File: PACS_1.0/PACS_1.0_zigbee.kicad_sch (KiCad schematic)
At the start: 9 parts

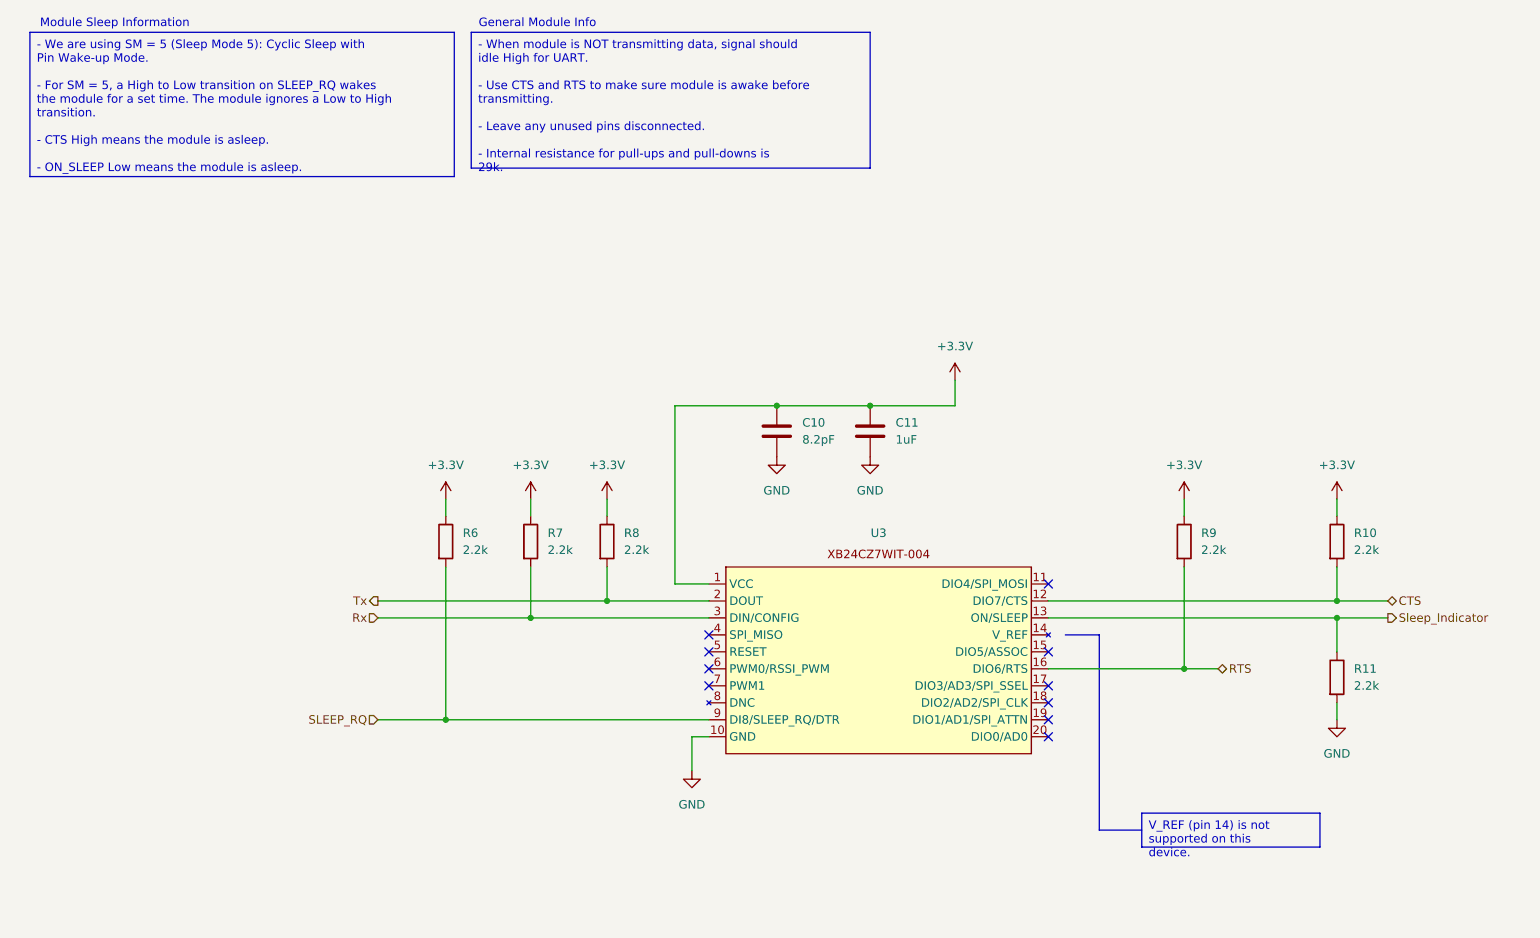
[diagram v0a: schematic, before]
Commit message: Finished 1.0 (NO INA INCLUDED)
Finished PACS 1.0 sheets, Power sheet needs considerations, no INA yet.
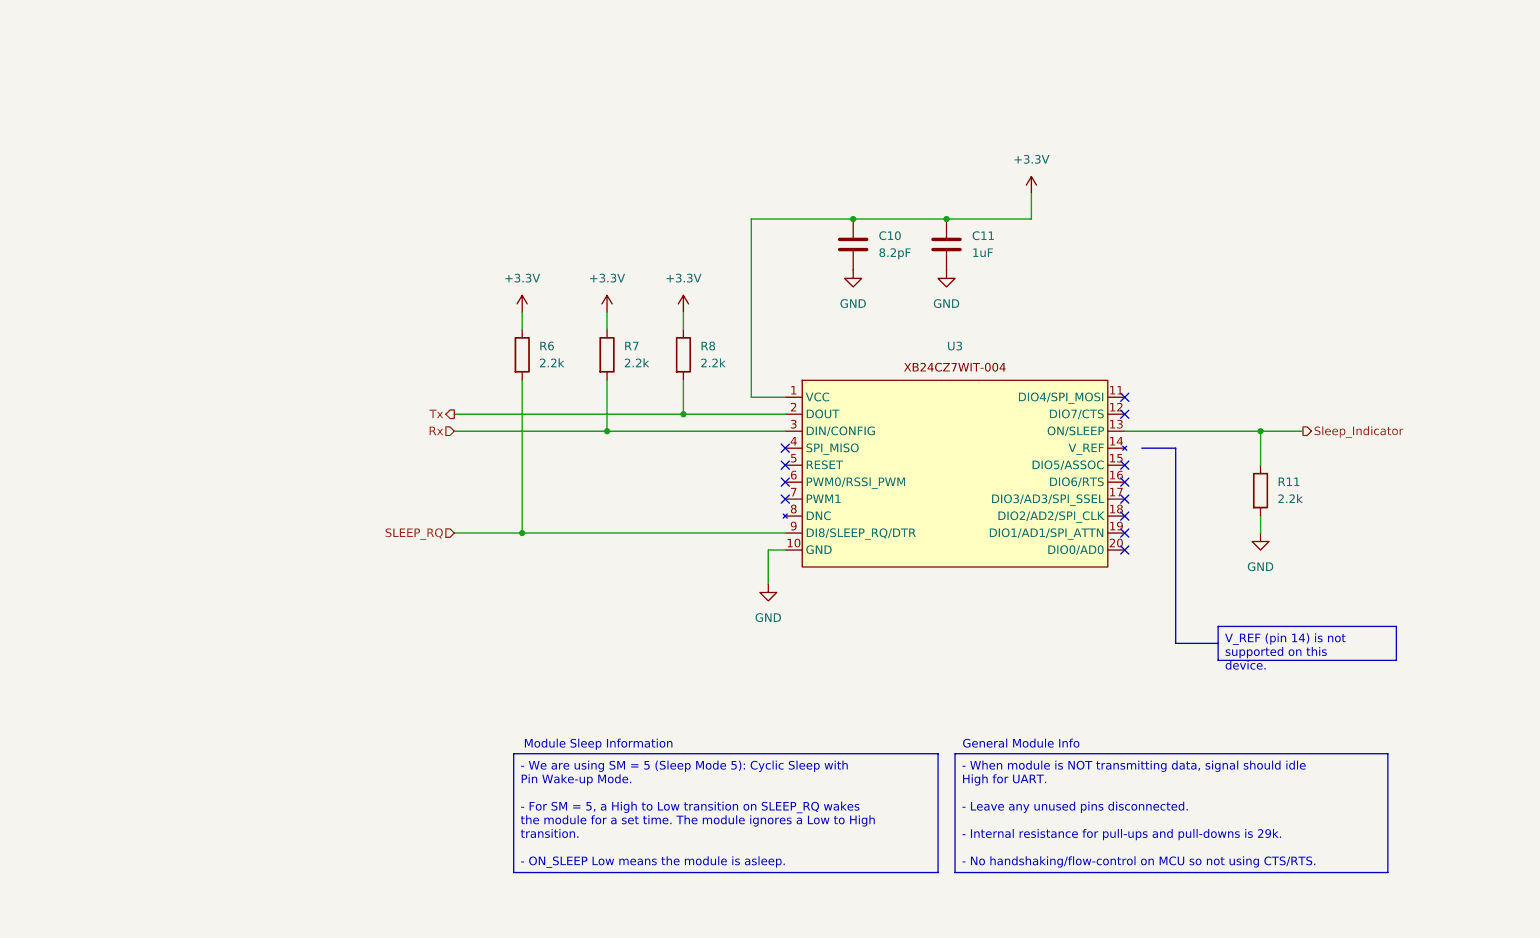
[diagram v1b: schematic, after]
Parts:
- removed R10, R9: 2.2k, symbol Device:R
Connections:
- net CTS: no longer names the net of U3.12 (DIO7/CTS)
- net RTS: no longer names the net of U3.16 (DIO6/RTS)
- no-connect marks 10 -> 12
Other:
- company: (none) -> PACS
- title: (none) -> Zigbee Module
- moved on the sheet: C10, C11, R11, R6, R7, R8, U3

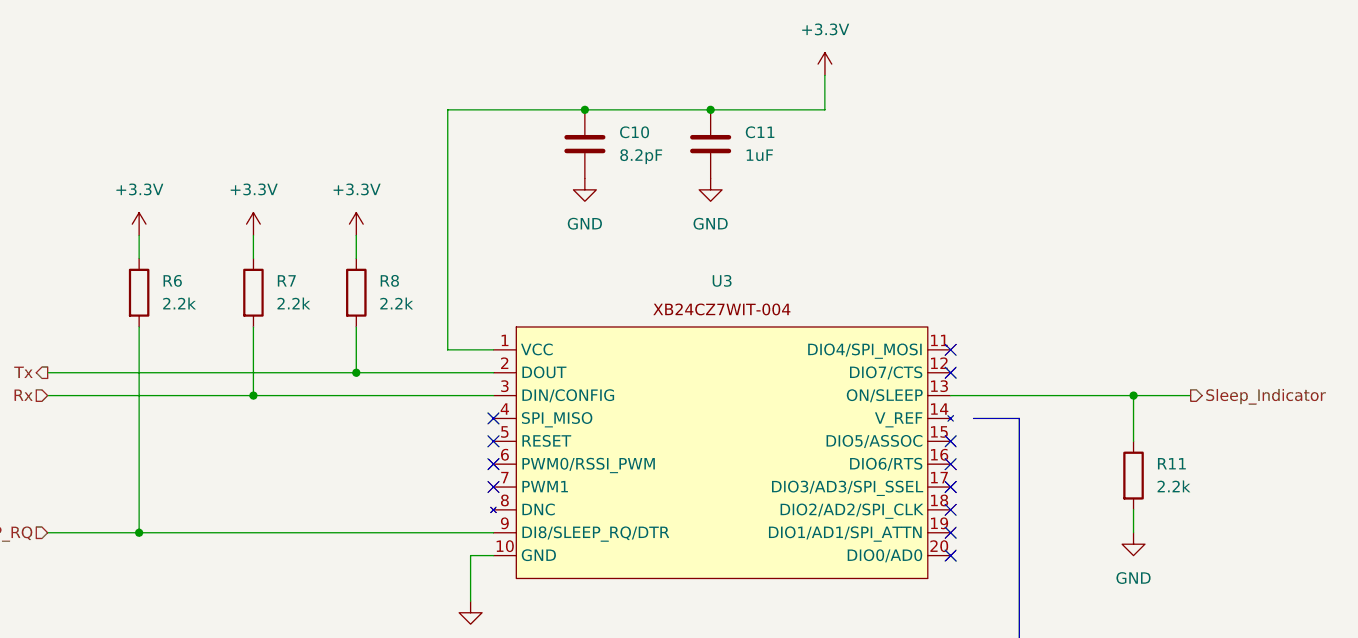
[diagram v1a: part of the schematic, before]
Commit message: Changed reference for Components
C8 to C2 (AS EXAMPLE)
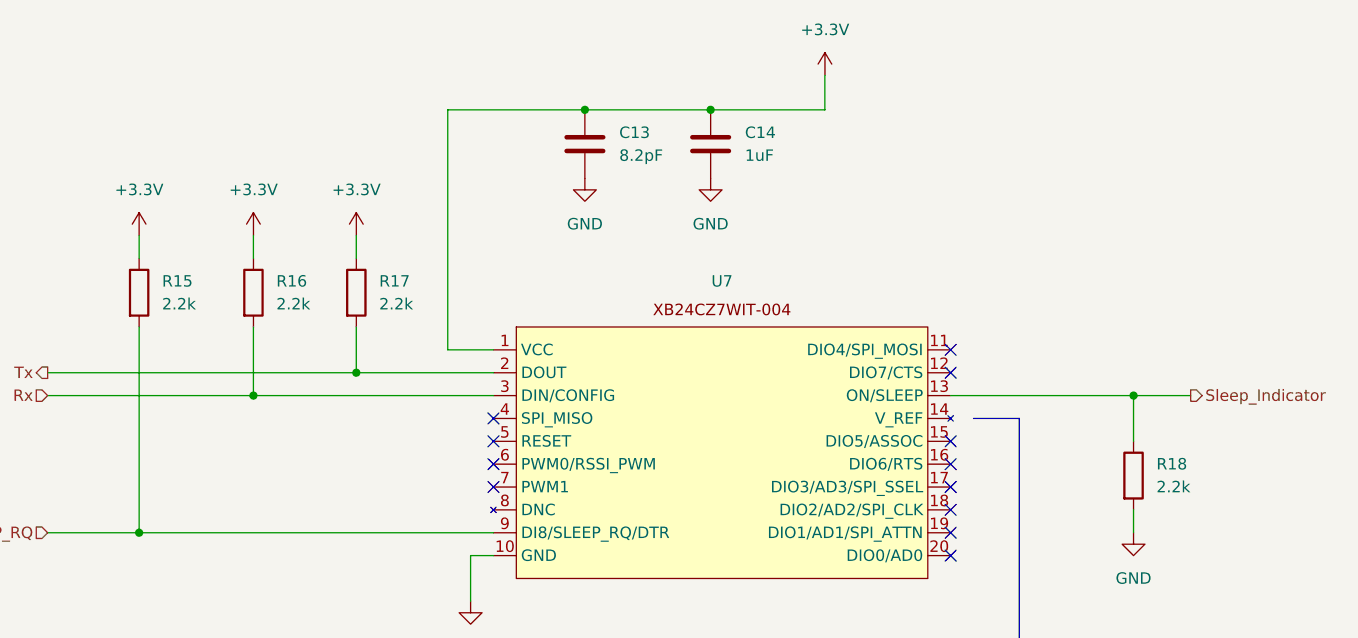
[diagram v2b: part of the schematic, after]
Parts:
- renumbered C10 to C13, C11 to C14, R6 to R15, R7 to R16, R8 to R17, R11 to R18, U3 to U7
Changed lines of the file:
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@@
 		(dnp no)
 		(fields_autoplaced yes)
-		(property "Reference" "#PWR014"
+		(property "Reference" "#PWR036"
 			(at 163.83 45.72 0)
 			(effects
@@
 			(project "PACS_1.0"
 				(path "/6996cbc8-fffb-40fd-8350-2bb7d19e6e7a/e639144c-29e9-4864-978f-8ae17353cb56"
-					(reference "#PWR014")
+					(reference "#PWR036")
 					(unit 1)
 				)
@@
 		(dnp no)
 		(fields_autoplaced yes)
-		(property "Reference" "#PWR024"
+		(property "Reference" "#PWR031"
 			(at 100.33 63.5 0)
 			(effects
@@
 			(project "PACS_1.0"
 				(path "/6996cbc8-fffb-40fd-8350-2bb7d19e6e7a/e639144c-29e9-4864-978f-8ae17353cb56"
-					(reference "#PWR024")
+					(reference "#PWR031")
 					(unit 1)
 				)
@@
 		(dnp no)
 		(fields_autoplaced yes)
-		(property "Reference" "C10"
+		(property "Reference" "C13"
 			(at 140.97 48.2599 0)
 			(effects
@@
 			(project "PACS_1.0"
 				(path "/6996cbc8-fffb-40fd-8350-2bb7d19e6e7a/e639144c-29e9-4864-978f-8ae17353cb56"
-					(reference "C10")
+					(reference "C13")
 					(unit 1)
 				)
@@
 		(on_board yes)
 		(dnp no)
-		(property "Reference" "U3"
+		(property "Reference" "U7"
 			(at 152.4 64.77 0)
 			(effects
@@
 			(project ""
 				(path "/6996cbc8-fffb-40fd-8350-2bb7d19e6e7a/e639144c-29e9-4864-978f-8ae17353cb56"
-					(reference "U3")
+					(reference "U7")
 					(unit 1)
 				)
@@
 		(dnp no)
 		(fields_autoplaced yes)
-		(property "Reference" "#PWR031"
+		(property "Reference" "#PWR037"
 			(at 198.12 99.06 0)
 			(effects
@@
 			(project "PACS_1.0"
 				(path "/6996cbc8-fffb-40fd-8350-2bb7d19e6e7a/e639144c-29e9-4864-978f-8ae17353cb56"
-					(reference "#PWR031")
+					(reference "#PWR037")
 					(unit 1)
 				)
@@
 		(dnp no)
 		(fields_autoplaced yes)
-		(property "Reference" "#PWR026"
+		(property "Reference" "#PWR035"
 			(at 151.13 59.69 0)
 			(effects
@@
 			(project "PACS_1.0"
 				(path "/6996cbc8-fffb-40fd-8350-2bb7d19e6e7a/e639144c-29e9-4864-978f-8ae17353cb56"
-					(reference "#PWR026")
+					(reference "#PWR035")
 					(unit 1)
 				)
@@
 		(dnp no)
 		(fields_autoplaced yes)
-		(property "Reference" "R7"
+		(property "Reference" "R16"
 			(at 102.87 64.7699 0)
 			(effects
@@
 			(project "PACS_1.0"
 				(path "/6996cbc8-fffb-40fd-8350-2bb7d19e6e7a/e639144c-29e9-4864-978f-8ae17353cb56"
-					(reference "R7")
+					(reference "R16")
 					(unit 1)
 				)
@@
 		(dnp no)
 		(fields_autoplaced yes)
-		(property "Reference" "C11"
+		(property "Reference" "C14"
 			(at 154.94 48.2599 0)
 			(effects
@@
 			(project "PACS_1.0"
 				(path "/6996cbc8-fffb-40fd-8350-2bb7d19e6e7a/e639144c-29e9-4864-978f-8ae17353cb56"
-					(reference "C11")
+					(reference "C14")
 					(unit 1)
 				)
@@
 		(dnp no)
 		(fields_autoplaced yes)
-		(property "Reference" "#PWR015"
+		(property "Reference" "#PWR033"
 			(at 124.46 106.68 0)
 			(effects
@@
 			(project ""
 				(path "/6996cbc8-fffb-40fd-8350-2bb7d19e6e7a/e639144c-29e9-4864-978f-8ae17353cb56"
-					(reference "#PWR015")
+					(reference "#PWR033")
 					(unit 1)
 				)
@@
 		(dnp no)
 		(fields_autoplaced yes)
-		(property "Reference" "R8"
+		(property "Reference" "R17"
 			(at 114.3 64.7699 0)
 			(effects
@@
 			(project "PACS_1.0"
 				(path "/6996cbc8-fffb-40fd-8350-2bb7d19e6e7a/e639144c-29e9-4864-978f-8ae17353cb56"
-					(reference "R8")
+					(reference "R17")
 					(unit 1)
 				)
@@
 		(dnp no)
 		(fields_autoplaced yes)
-		(property "Reference" "R6"
+		(property "Reference" "R15"
 			(at 90.17 64.7699 0)
 			(effects
@@
 			(project "PACS_1.0"
 				(path "/6996cbc8-fffb-40fd-8350-2bb7d19e6e7a/e639144c-29e9-4864-978f-8ae17353cb56"
-					(reference "R6")
+					(reference "R15")
 					(unit 1)
 				)
@@
 		(dnp no)
 		(fields_autoplaced yes)
-		(property "Reference" "R11"
+		(property "Reference" "R18"
 			(at 200.66 85.0899 0)
 			(effects
@@
 			(project "PACS_1.0"
 				(path "/6996cbc8-fffb-40fd-8350-2bb7d19e6e7a/e639144c-29e9-4864-978f-8ae17353cb56"
-					(reference "R11")
+					(reference "R18")
 					(unit 1)
 				)
@@
 		(dnp no)
 		(fields_autoplaced yes)
-		(property "Reference" "#PWR023"
+		(property "Reference" "#PWR032"
 			(at 111.76 63.5 0)
 			(effects
@@
 			(project "PACS_1.0"
 				(path "/6996cbc8-fffb-40fd-8350-2bb7d19e6e7a/e639144c-29e9-4864-978f-8ae17353cb56"
-					(reference "#PWR023")
+					(reference "#PWR032")
 					(unit 1)
 				)
@@
 		(dnp no)
 		(fields_autoplaced yes)
-		(property "Reference" "#PWR025"
+		(property "Reference" "#PWR034"
 			(at 137.16 59.69 0)
 			(effects
@@
 			(project "PACS_1.0"
 				(path "/6996cbc8-fffb-40fd-8350-2bb7d19e6e7a/e639144c-29e9-4864-978f-8ae17353cb56"
-					(reference "#PWR025")
-					(unit 1)
-				)
+					(reference "#PWR034")
+					(unit 1)
+				)

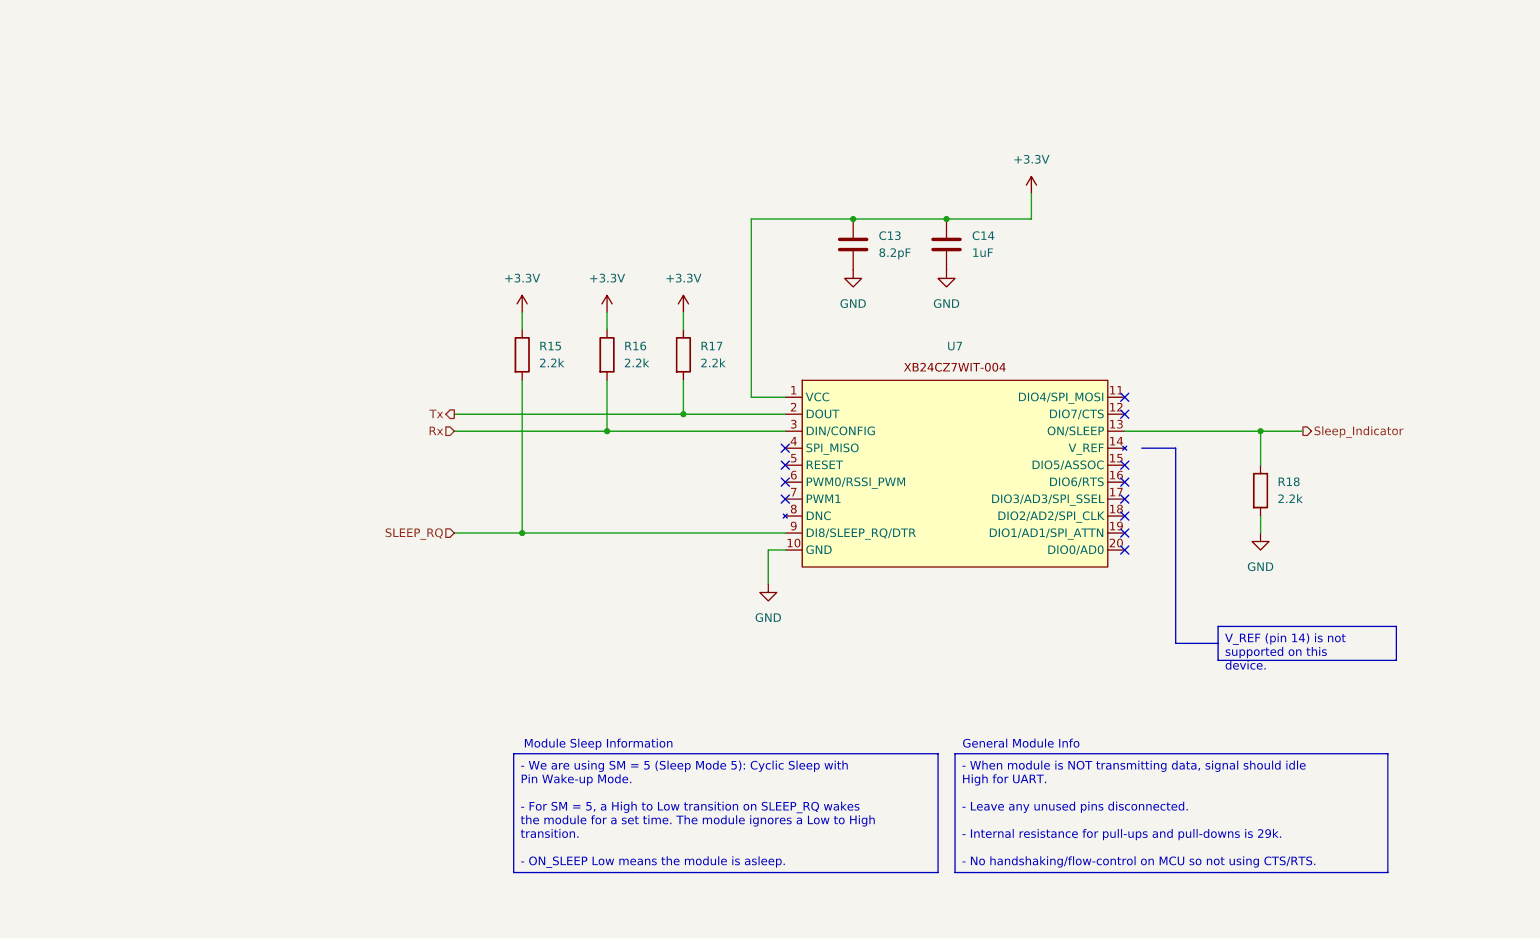
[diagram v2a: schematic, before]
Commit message: Added Boxes and fixed PDF
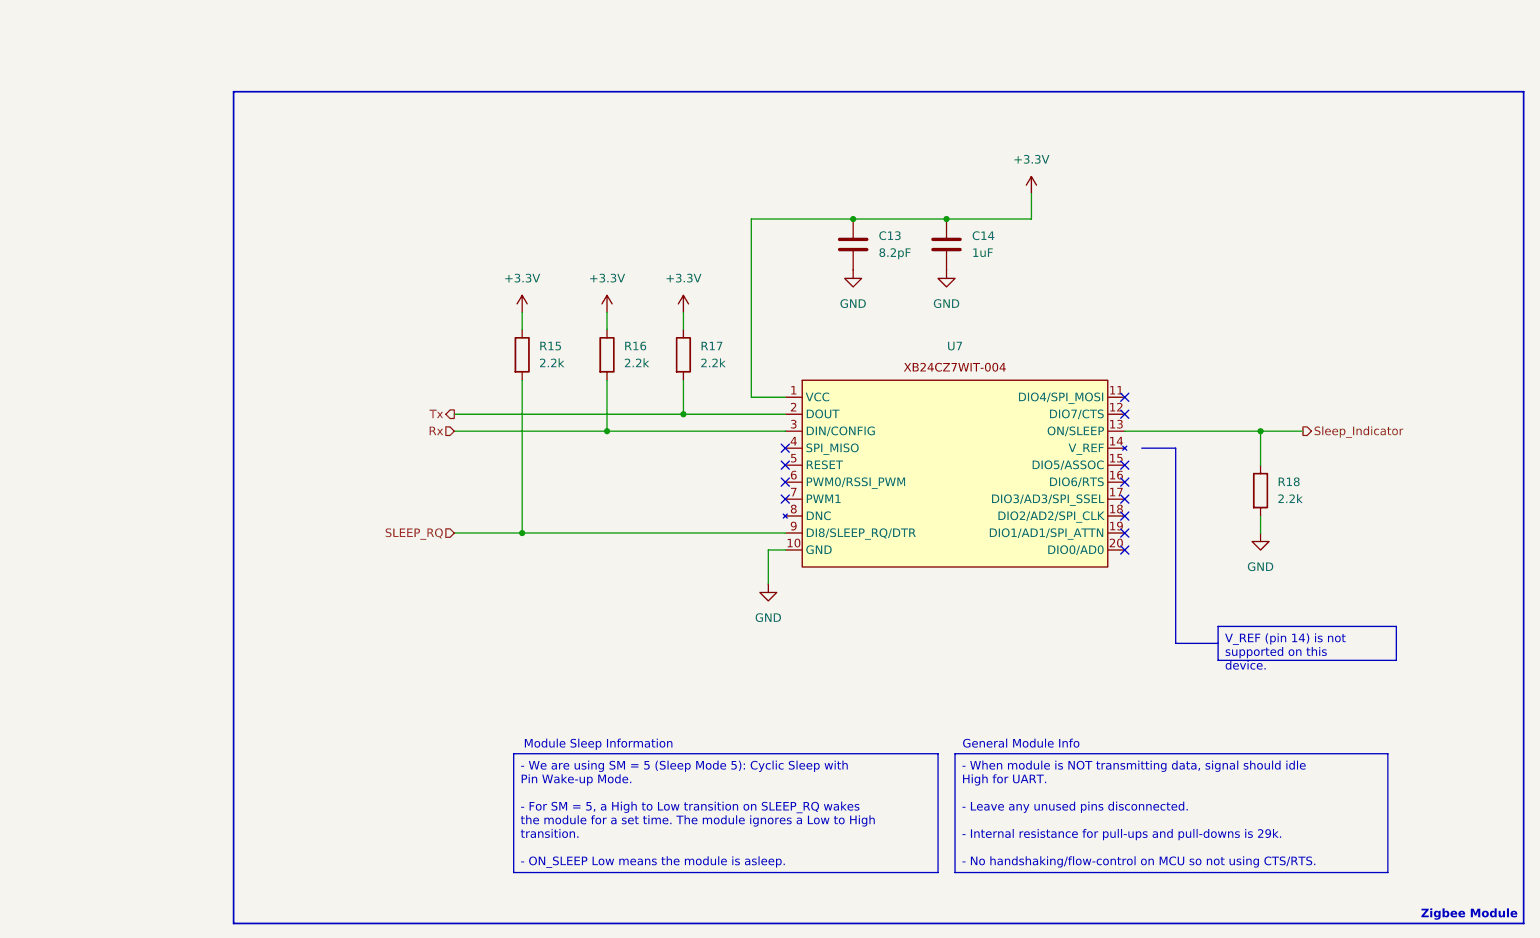
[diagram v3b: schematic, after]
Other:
- note added: "Zigbee Module"
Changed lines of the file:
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@@
+		)
+	)
+	(rectangle
+		(start 44.45 26.67)
+		(end 237.49 151.13)
+		(stroke
+			(width 0.254)
+			(type default)
+		)
+		(fill
+			(type none)
 		)
 	)
@@
 		)
 	)
+	(text "Zigbee Module"
+		(exclude_from_sim no)
+		(at 229.362 149.86 0)
+		(effects
+			(font
+				(size 1.27 1.27)
+				(thickness 0.254)
+				(bold yes)
+			)
+		)
+	)

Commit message: Updated footprints for caps and resistors
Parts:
- C13: footprint (none) -> Capacitor_SMD:C_0402_1005Metric
- C14: footprint (none) -> Capacitor_SMD:C_0603_1608Metric
- R15, R16, R17, R18: footprint (none) -> Resistor_SMD:R_0402_1005Metric
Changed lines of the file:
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@@
 			)
 		)
-		(property "Footprint" ""
+		(property "Footprint" "Capacitor_SMD:C_0402_1005Metric"
 			(at 138.1252 53.34 0)
 			(effects
@@
 			)
 		)
-		(property "Footprint" ""
+		(property "Footprint" "Resistor_SMD:R_0402_1005Metric"
 			(at 98.552 66.04 90)
 			(effects
@@
 			)
 		)
-		(property "Footprint" ""
+		(property "Footprint" "Capacitor_SMD:C_0603_1608Metric"
 			(at 152.0952 53.34 0)
 			(effects
@@
 			)
 		)
-		(property "Footprint" ""
+		(property "Footprint" "Resistor_SMD:R_0402_1005Metric"
 			(at 109.982 66.04 90)
 			(effects
@@
 			)
 		)
-		(property "Footprint" ""
+		(property "Footprint" "Resistor_SMD:R_0402_1005Metric"
 			(at 85.852 66.04 90)
 			(effects
@@
 			)
 		)
-		(property "Footprint" ""
+		(property "Footprint" "Resistor_SMD:R_0402_1005Metric"
 			(at 196.342 86.36 90)
 			(effects

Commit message: Started the PCB design
added several footprints, need to find footprint for Xbee, need to add traces for GND and power
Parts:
- U7: value ~ -> XB24CZ7WIT-004
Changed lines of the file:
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@@
 			)
 		)
-		(property "Value" "~"
-			(at 152.4 64.77 0)
+		(property "Value" "XB24CZ7WIT-004"
+			(at 152.4 67.31 0)
 			(effects
 				(font

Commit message: FINISHED PCB DESIGN
must double check that the dimensions for XBee footprint are correct
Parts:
- U7: footprint (none) -> RF_Module:XB24CZ7WIT-004
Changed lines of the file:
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@@
 			)
 		)
-		(property "Footprint" ""
+		(property "Footprint" "RF_Module:XB24CZ7WIT-004"
 			(at 118.745 147.955 0)
 			(effects
